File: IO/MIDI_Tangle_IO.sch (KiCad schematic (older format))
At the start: 54 parts, among them J1 Conn_01x08_Male, J10 AudioJack2, J11 AudioJack2, J12 AudioJack2, J13 AudioJack2, J14 AudioJack2, J15 AudioJack2, J16 AudioJack2, J17 AudioJack2, J18 AudioJack2, J19 AudioJack2, J2 Conn_01x08_Male, J20 AudioJack2, J3 Conn_01x08_Male, J4 Conn_01x08_Male, J5 AudioJack2, J6 AudioJack2, J7 AudioJack2, J8 AudioJack2, J9 AudioJack2, SW1 SW_SPST, SW2 SW_SPST, SW3 SW_SPST, SW4 SW_SPST, SW5 SW_SPST, SW6 SW_SPST, SW7 SW_SPST, SW8 SW_SPST

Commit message: Add custom footprints and symbols
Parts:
- D1: footprint LED_THT:LED_D3.0mm -> Custom_FP:LED_D3.0mm_NoCourtyard
- D2, D3, D4, D5, D6, D7, D8, D9: footprint LED_THT:LED_D5.0mm_FlatTop -> Custom_FP:LED_D5.0mm_FlatTop_NoCourtyard
- J10, J11, J12, J13, J14, J15, J16, J17, J18, J19, J20, J5, J6, J7, J8, J9: footprint CustomLib:PJ398SM -> Custom_FP:PJ398SM
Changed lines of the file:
@@
 F 0 "J13" H 10182 1275 50  0000 C CNN
 F 1 "AudioJack2" H 10182 1184 50  0000 C CNN
-F 2 "CustomLib:PJ398SM" H 10150 950 50  0001 C CNN
+F 2 "Custom_FP:PJ398SM" H 10150 950 50  0001 C CNN
 F 3 "~" H 10150 950 50  0001 C CNN
 	1    10150 950
@@
 F 0 "J14" H 10182 2125 50  0000 C CNN
 F 1 "AudioJack2" H 10182 2034 50  0000 C CNN
-F 2 "CustomLib:PJ398SM" H 10150 1800 50  0001 C CNN
+F 2 "Custom_FP:PJ398SM" H 10150 1800 50  0001 C CNN
 F 3 "~" H 10150 1800 50  0001 C CNN
 	1    10150 1800
@@
 F 0 "J15" H 10182 2975 50  0000 C CNN
 F 1 "AudioJack2" H 10182 2884 50  0000 C CNN
-F 2 "CustomLib:PJ398SM" H 10150 2650 50  0001 C CNN
+F 2 "Custom_FP:PJ398SM" H 10150 2650 50  0001 C CNN
 F 3 "~" H 10150 2650 50  0001 C CNN
 	1    10150 2650
@@
 F 0 "J16" H 10182 3825 50  0000 C CNN
 F 1 "AudioJack2" H 10182 3734 50  0000 C CNN
-F 2 "CustomLib:PJ398SM" H 10150 3500 50  0001 C CNN
+F 2 "Custom_FP:PJ398SM" H 10150 3500 50  0001 C CNN
 F 3 "~" H 10150 3500 50  0001 C CNN
 	1    10150 3500
@@
 F 0 "J17" H 8282 1275 50  0000 C CNN
 F 1 "AudioJack2" H 8282 1184 50  0000 C CNN
-F 2 "CustomLib:PJ398SM" H 8250 950 50  0001 C CNN
+F 2 "Custom_FP:PJ398SM" H 8250 950 50  0001 C CNN
 F 3 "~" H 8250 950 50  0001 C CNN
 	1    8250 950
@@
 F 0 "J18" H 8282 2125 50  0000 C CNN
 F 1 "AudioJack2" H 8282 2034 50  0000 C CNN
-F 2 "CustomLib:PJ398SM" H 8250 1800 50  0001 C CNN
+F 2 "Custom_FP:PJ398SM" H 8250 1800 50  0001 C CNN
 F 3 "~" H 8250 1800 50  0001 C CNN
 	1    8250 1800
@@
 F 0 "J19" H 8282 2975 50  0000 C CNN
 F 1 "AudioJack2" H 8282 2884 50  0000 C CNN
-F 2 "CustomLib:PJ398SM" H 8250 2650 50  0001 C CNN
+F 2 "Custom_FP:PJ398SM" H 8250 2650 50  0001 C CNN
 F 3 "~" H 8250 2650 50  0001 C CNN
 	1    8250 2650
@@
 F 0 "J20" H 8282 3825 50  0000 C CNN
 F 1 "AudioJack2" H 8282 3734 50  0000 C CNN
-F 2 "CustomLib:PJ398SM" H 8250 3500 50  0001 C CNN
+F 2 "Custom_FP:PJ398SM" H 8250 3500 50  0001 C CNN
 F 3 "~" H 8250 3500 50  0001 C CNN
 	1    8250 3500
@@
 F 0 "D9" H 8200 3650 50  0000 C CNN
 F 1 "LED_RG" H 8350 3950 50  0000 C CNN
-F 2 "LED_THT:LED_D5.0mm_FlatTop" H 7950 3800 50  0001 C CNN
+F 2 "Custom_FP:LED_D5.0mm_FlatTop_NoCourtyard" H 7950 3800 50  0001 C CNN
 F 3 "~" H 7950 3800 50  0001 C CNN
 	1    7950 3800
@@
 F 0 "D8" H 8200 2800 50  0000 C CNN
 F 1 "LED_RG" H 8350 3100 50  0000 C CNN
-F 2 "LED_THT:LED_D5.0mm_FlatTop" H 7950 2950 50  0001 C CNN
+F 2 "Custom_FP:LED_D5.0mm_FlatTop_NoCourtyard" H 7950 2950 50  0001 C CNN
 F 3 "~" H 7950 2950 50  0001 C CNN
 	1    7950 2950
@@
 F 0 "D7" H 8200 1950 50  0000 C CNN
 F 1 "LED_RG" H 8350 2250 50  0000 C CNN
-F 2 "LED_THT:LED_D5.0mm_FlatTop" H 7950 2100 50  0001 C CNN
+F 2 "Custom_FP:LED_D5.0mm_FlatTop_NoCourtyard" H 7950 2100 50  0001 C CNN
 F 3 "~" H 7950 2100 50  0001 C CNN
 	1    7950 2100
@@
 F 0 "D6" H 8200 1100 50  0000 C CNN
 F 1 "LED_RG" H 8350 1400 50  0000 C CNN
-F 2 "LED_THT:LED_D5.0mm_FlatTop" H 7950 1250 50  0001 C CNN
+F 2 "Custom_FP:LED_D5.0mm_FlatTop_NoCourtyard" H 7950 1250 50  0001 C CNN
 F 3 "~" H 7950 1250 50  0001 C CNN
 	1    7950 1250
@@
 F 0 "D5" H 10100 3650 50  0000 C CNN
 F 1 "LED_RG" H 10250 3950 50  0000 C CNN
-F 2 "LED_THT:LED_D5.0mm_FlatTop" H 9850 3800 50  0001 C CNN
+F 2 "Custom_FP:LED_D5.0mm_FlatTop_NoCourtyard" H 9850 3800 50  0001 C CNN
 F 3 "~" H 9850 3800 50  0001 C CNN
 	1    9850 3800
@@
 F 0 "D4" H 10100 2800 50  0000 C CNN
 F 1 "LED_RG" H 10250 3100 50  0000 C CNN
-F 2 "LED_THT:LED_D5.0mm_FlatTop" H 9850 2950 50  0001 C CNN
+F 2 "Custom_FP:LED_D5.0mm_FlatTop_NoCourtyard" H 9850 2950 50  0001 C CNN
 F 3 "~" H 9850 2950 50  0001 C CNN
 	1    9850 2950
@@
 F 0 "D3" H 10100 1950 50  0000 C CNN
 F 1 "LED_RG" H 10250 2250 50  0000 C CNN
-F 2 "LED_THT:LED_D5.0mm_FlatTop" H 9850 2100 50  0001 C CNN
+F 2 "Custom_FP:LED_D5.0mm_FlatTop_NoCourtyard" H 9850 2100 50  0001 C CNN
 F 3 "~" H 9850 2100 50  0001 C CNN
 	1    9850 2100
@@
 F 0 "D2" H 10100 1100 50  0000 C CNN
 F 1 "LED_RG" H 10250 1400 50  0000 C CNN
-F 2 "LED_THT:LED_D5.0mm_FlatTop" H 9850 1250 50  0001 C CNN
+F 2 "Custom_FP:LED_D5.0mm_FlatTop_NoCourtyard" H 9850 1250 50  0001 C CNN
 F 3 "~" H 9850 1250 50  0001 C CNN
 	1    9850 1250
@@
 F 0 "J5" H 6132 1925 50  0000 C CNN
 F 1 "AudioJack2" H 6132 1834 50  0000 C CNN
-F 2 "CustomLib:PJ398SM" H 6100 1600 50  0001 C CNN
+F 2 "Custom_FP:PJ398SM" H 6100 1600 50  0001 C CNN
 F 3 "~" H 6100 1600 50  0001 C CNN
 	1    6100 1600
@@
 F 0 "J6" H 6132 2425 50  0000 C CNN
 F 1 "AudioJack2" H 6132 2334 50  0000 C CNN
-F 2 "CustomLib:PJ398SM" H 6100 2100 50  0001 C CNN
+F 2 "Custom_FP:PJ398SM" H 6100 2100 50  0001 C CNN
 F 3 "~" H 6100 2100 50  0001 C CNN
 	1    6100 2100
@@
 F 0 "J7" H 6132 2925 50  0000 C CNN
 F 1 "AudioJack2" H 6132 2834 50  0000 C CNN
-F 2 "CustomLib:PJ398SM" H 6100 2600 50  0001 C CNN
+F 2 "Custom_FP:PJ398SM" H 6100 2600 50  0001 C CNN
 F 3 "~" H 6100 2600 50  0001 C CNN
 	1    6100 2600
@@
 F 0 "J8" H 6132 3425 50  0000 C CNN
 F 1 "AudioJack2" H 6132 3334 50  0000 C CNN
-F 2 "CustomLib:PJ398SM" H 6100 3100 50  0001 C CNN
+F 2 "Custom_FP:PJ398SM" H 6100 3100 50  0001 C CNN
 F 3 "~" H 6100 3100 50  0001 C CNN
 	1    6100 3100
@@
 F 0 "J9" H 6132 3925 50  0000 C CNN
 F 1 "AudioJack2" H 6132 3834 50  0000 C CNN
-F 2 "CustomLib:PJ398SM" H 6100 3600 50  0001 C CNN
+F 2 "Custom_FP:PJ398SM" H 6100 3600 50  0001 C CNN
 F 3 "~" H 6100 3600 50  0001 C CNN
 	1    6100 3600
@@
 F 0 "J10" H 6132 4425 50  0000 C CNN
 F 1 "AudioJack2" H 6132 4334 50  0000 C CNN
-F 2 "CustomLib:PJ398SM" H 6100 4100 50  0001 C CNN
+F 2 "Custom_FP:PJ398SM" H 6100 4100 50  0001 C CNN
 F 3 "~" H 6100 4100 50  0001 C CNN
 	1    6100 4100
@@
 F 0 "J11" H 6132 4925 50  0000 C CNN
 F 1 "AudioJack2" H 6132 4834 50  0000 C CNN
-F 2 "CustomLib:PJ398SM" H 6100 4600 50  0001 C CNN
+F 2 "Custom_FP:PJ398SM" H 6100 4600 50  0001 C CNN
 F 3 "~" H 6100 4600 50  0001 C CNN
 	1    6100 4600
@@
 F 0 "J12" H 6132 5425 50  0000 C CNN
 F 1 "AudioJack2" H 6132 5334 50  0000 C CNN
-F 2 "CustomLib:PJ398SM" H 6100 5100 50  0001 C CNN
+F 2 "Custom_FP:PJ398SM" H 6100 5100 50  0001 C CNN
 F 3 "~" H 6100 5100 50  0001 C CNN
 	1    6100 5100
@@
 F 0 "D1" V 3689 4632 50  0000 R CNN
 F 1 "LED" V 3598 4632 50  0000 R CNN
-F 2 "LED_THT:LED_D3.0mm" H 3650 4750 50  0001 C CNN
+F 2 "Custom_FP:LED_D3.0mm_NoCourtyard" H 3650 4750 50  0001 C CNN
 F 3 "~" H 3650 4750 50  0001 C CNN
 	1    3650 4750

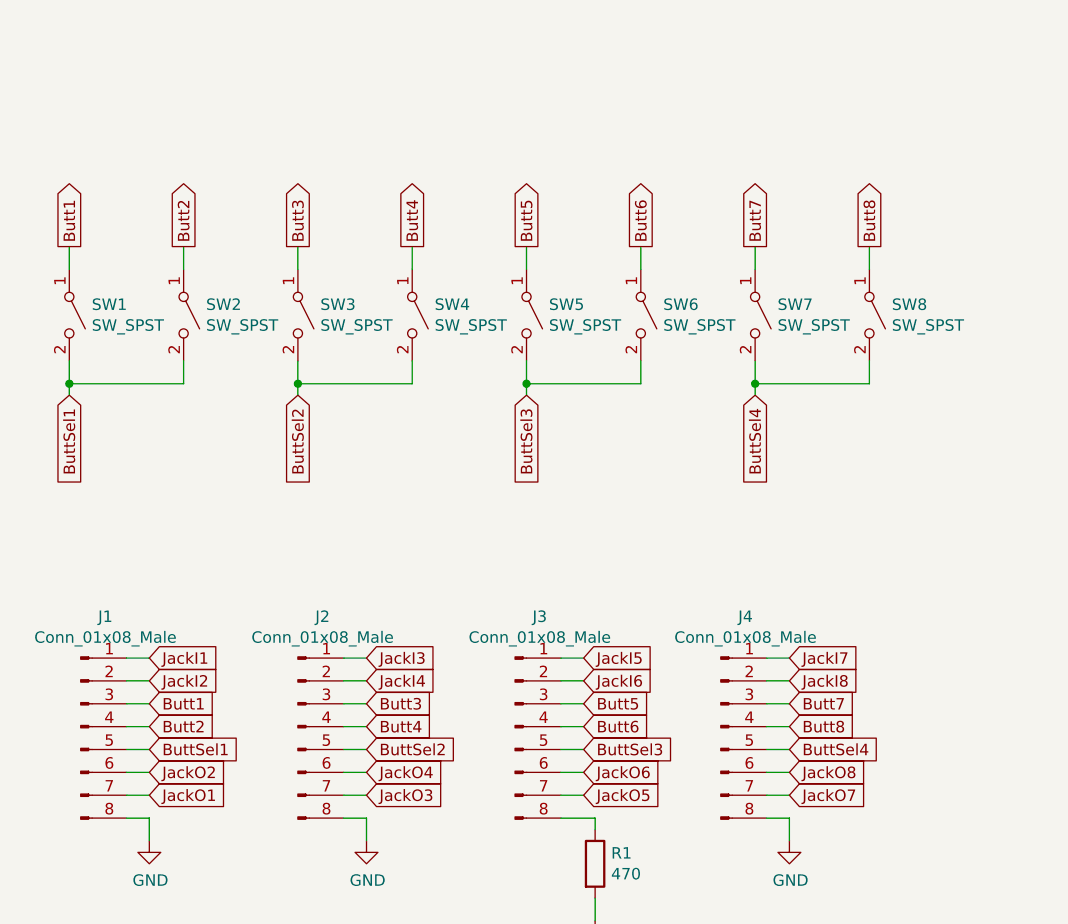
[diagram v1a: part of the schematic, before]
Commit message: Re-wire duplicate button signals
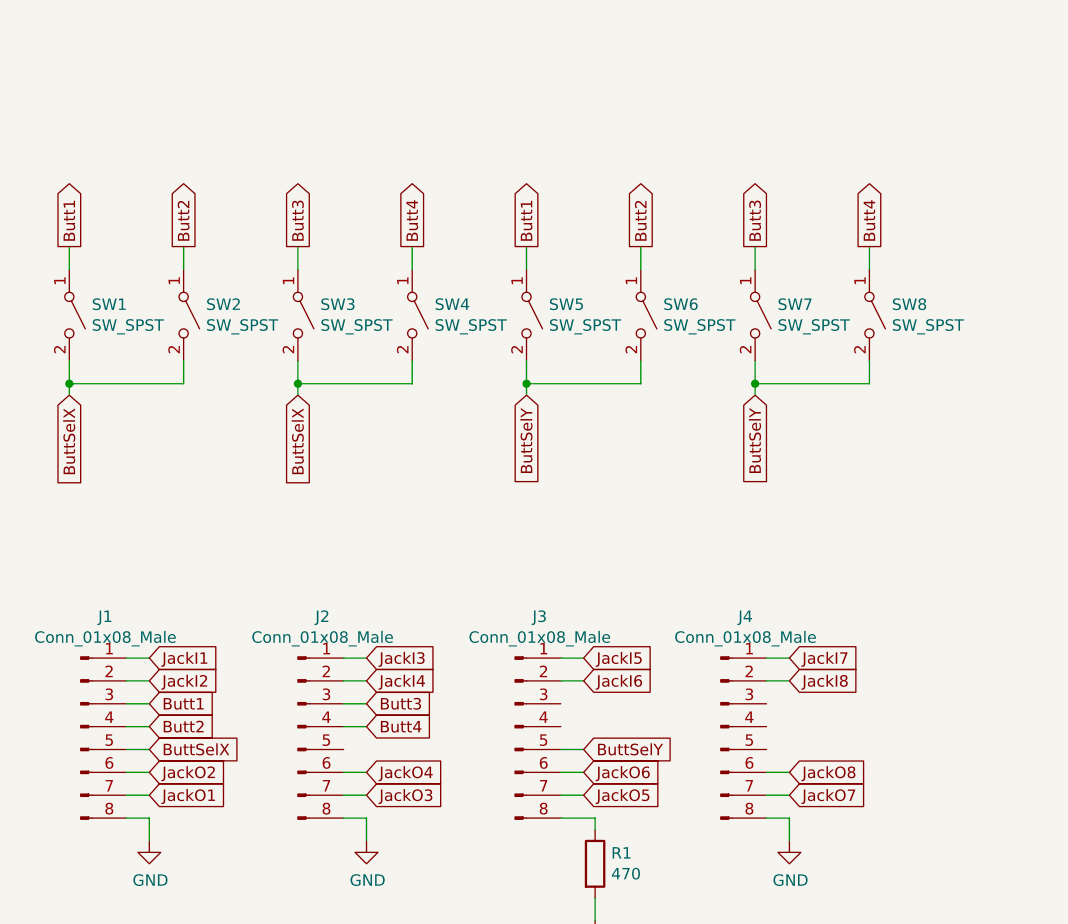
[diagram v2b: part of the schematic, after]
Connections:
- net Butt1: now also SW5.1 (A)
- net Butt2: now also SW6.1 (A)
- net Butt3: now also SW7.1 (A)
- net Butt4: now also SW8.1 (A)
- net Butt5: no longer names the net of J3.3 (Pin_3)
- net Butt5: no longer SW5.1 (A)
- net Butt6: no longer names the net of J3.4 (Pin_4)
- net Butt6: no longer SW6.1 (A)
- net Butt7: no longer names the net of J4.3 (Pin_3)
- net Butt7: no longer SW7.1 (A)
- net Butt8: no longer names the net of J4.4 (Pin_4)
- net Butt8: no longer SW8.1 (A)
- net ButtSel1 renamed ButtSelX
- net ButtSelX: now also SW3.2 (B), SW4.2 (B)
- removed net ButtSel2: J2.5 (Pin_5), SW3.2 (B), SW4.2 (B)
- net ButtSel3 renamed ButtSelY
- net ButtSelY: now also SW7.2 (B), SW8.2 (B)
- removed net ButtSel4: J4.5 (Pin_5), SW7.2 (B), SW8.2 (B)
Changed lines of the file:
@@
 Butt4
 Text GLabel 3350 1650 1    50   Output ~ 0
-Butt5
+Butt1
 Text GLabel 3850 1650 1    50   Output ~ 0
-Butt6
+Butt2
 Text GLabel 4350 1650 1    50   Output ~ 0
-Butt7
+Butt3
 Text GLabel 4850 1650 1    50   Output ~ 0
-Butt8
+Butt4
 Text GLabel 1700 3450 2    50   Input ~ 0
 JackI1
@@
 JackO2
 Text GLabel 1700 3850 2    50   Input ~ 0
-ButtSel1
+ButtSelX
 $Comp
 L power:GND #PWR0126
@@
 Text GLabel 2650 3950 2    50   Input ~ 0
 JackO4
-Text GLabel 2650 3850 2    50   Input ~ 0
-ButtSel2
 $Comp
 L power:GND #PWR0127
@@
 	2650 3950 2550 3950
 Wire Wire Line
-	2550 3850 2650 3850
-Wire Wire Line
 	2650 3750 2550 3750
 Wire Wire Line
@@
 Text GLabel 3600 3550 2    50   Input ~ 0
 JackI6
-Text GLabel 3600 3650 2    50   Input ~ 0
-Butt5
-Text GLabel 3600 3750 2    50   Input ~ 0
-Butt6
 Text GLabel 3600 4050 2    50   Input ~ 0
 JackO5
@@
 JackO6
 Text GLabel 3600 3850 2    50   Input ~ 0
-ButtSel3
+ButtSelY
 Wire Wire Line
 	3500 4050 3600 4050
@@
 Wire Wire Line
 	3500 3850 3600 3850
-Wire Wire Line
-	3600 3750 3500 3750
-Wire Wire Line
-	3500 3650 3600 3650
 Wire Wire Line
 	3600 3550 3500 3550
@@
 Text GLabel 4500 3550 2    50   Input ~ 0
 JackI8
-Text GLabel 4500 3650 2    50   Input ~ 0
-Butt7
-Text GLabel 4500 3750 2    50   Input ~ 0
-Butt8
 Text GLabel 4500 4050 2    50   Input ~ 0
 JackO7
 Text GLabel 4500 3950 2    50   Input ~ 0
 JackO8
-Text GLabel 4500 3850 2    50   Input ~ 0
-ButtSel4
 $Comp
 L power:GND #PWR0128
@@
 	4500 3950 4400 3950
 Wire Wire Line
-	4400 3850 4500 3850
-Wire Wire Line
-	4500 3750 4400 3750
-Wire Wire Line
-	4400 3650 4500 3650
-Wire Wire Line
 	4500 3550 4400 3550
 Wire Wire Line
 	4400 3450 4500 3450
 Text GLabel 1350 2300 3    50   Input ~ 0
-ButtSel1
+ButtSelX
 Wire Wire Line
 	1350 2300 1350 2250
@@
 Connection ~ 4350 2250
 Text GLabel 2350 2300 3    50   Input ~ 0
-ButtSel2
+ButtSelX
 Text GLabel 3350 2300 3    50   Input ~ 0
-ButtSel3
+ButtSelY
 Text GLabel 4350 2300 3    50   Input ~ 0
-ButtSel4
+ButtSelY
 $EndSCHEMATC

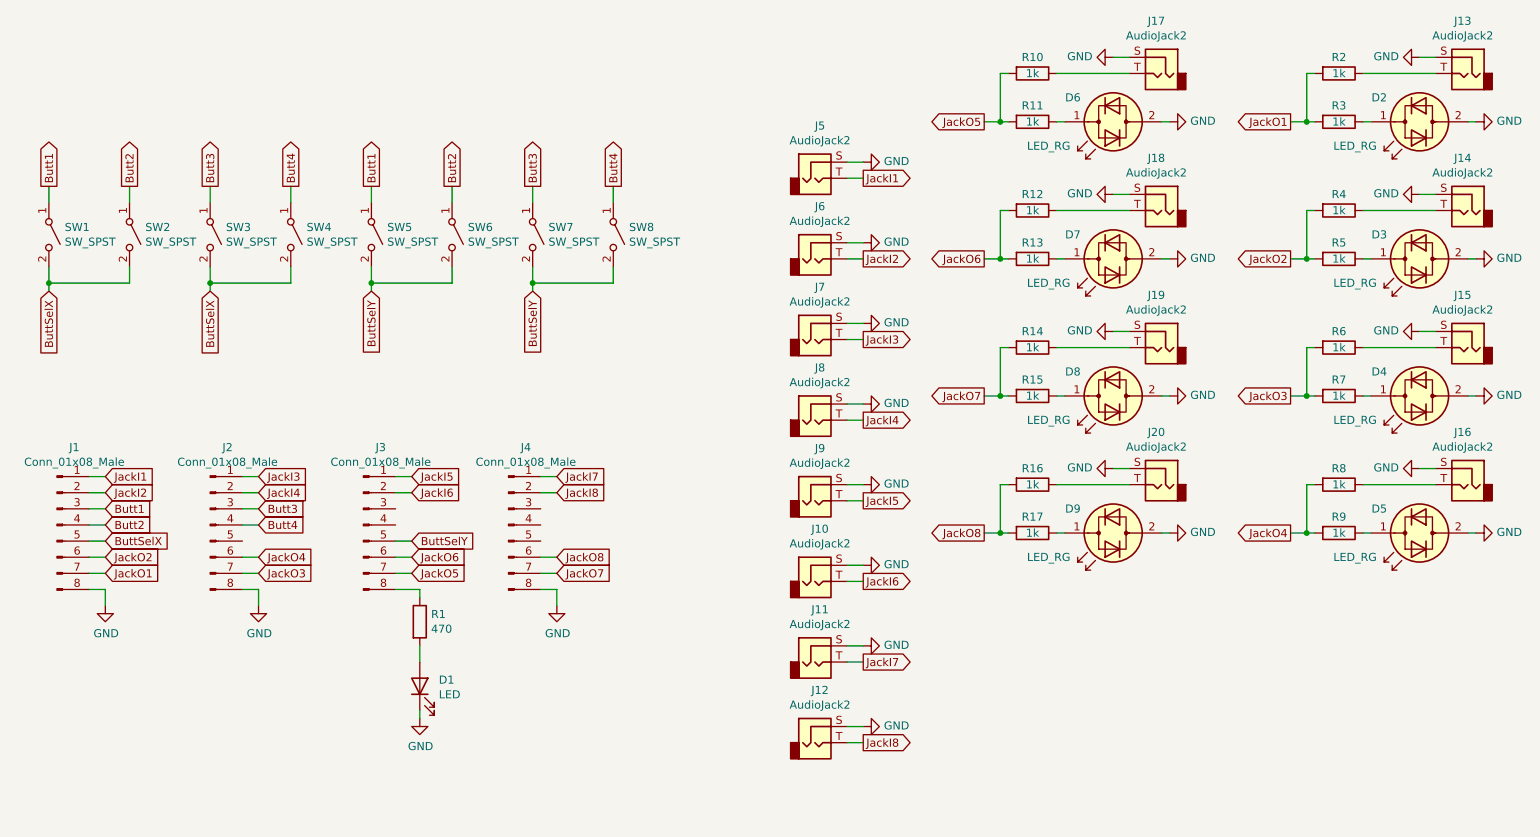
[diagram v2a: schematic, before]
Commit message: Add new bi-color LEDs
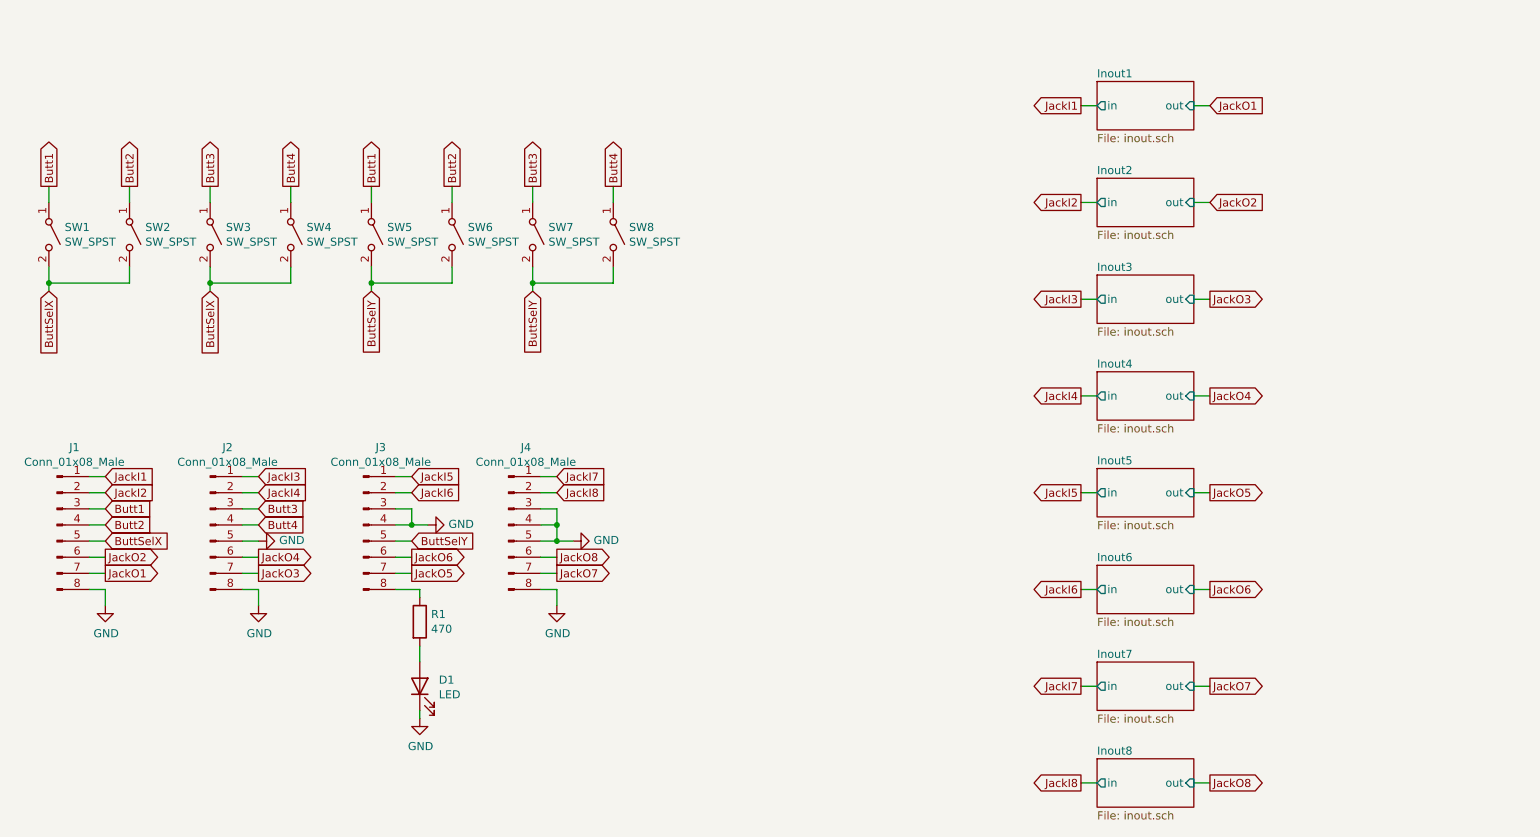
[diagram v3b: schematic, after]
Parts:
- removed D2, D3, D4, D5, D6, D7, D8, D9: LED_RG, Custom_FP:LED_D5.0mm_FlatTop_NoCourtyard, symbol Device:LED_Dual_2pin
- removed J10, J11, J12, J13, J14, J15, J16, J17, J18, J19, J20, J5, J6, J7, J8, J9: AudioJack2, Custom_FP:PJ398SM, symbol Connector:AudioJack2
- removed R10, R11, R12, R13, R14, R15, R16, R17, R2, R3, R4, R5, R6, R7, R8, R9: 1k, Resistor_SMD:R_0603_1608Metric, symbol Device:R
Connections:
- net GND: now also J2.5 (Pin_5), J3.3 (Pin_3), J3.4 (Pin_4), J4.3 (Pin_3), J4.4 (Pin_4), J4.5 (Pin_5)
